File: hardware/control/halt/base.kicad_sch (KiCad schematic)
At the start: 0 parts

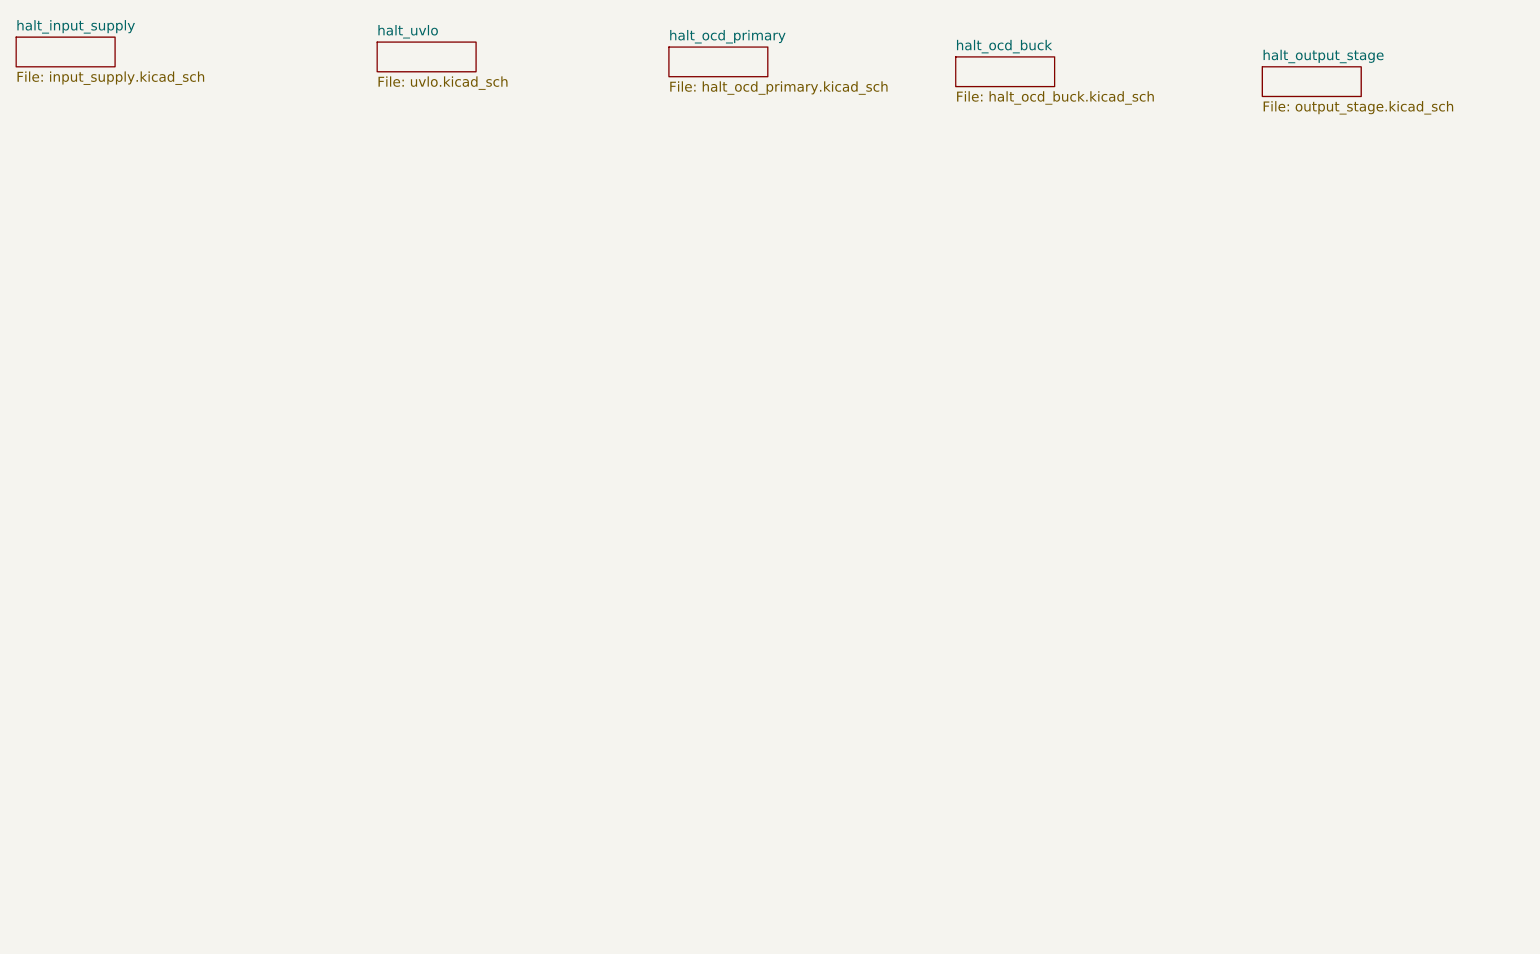
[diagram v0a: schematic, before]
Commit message: add progress on main drive controller and switch to hiearchical labels
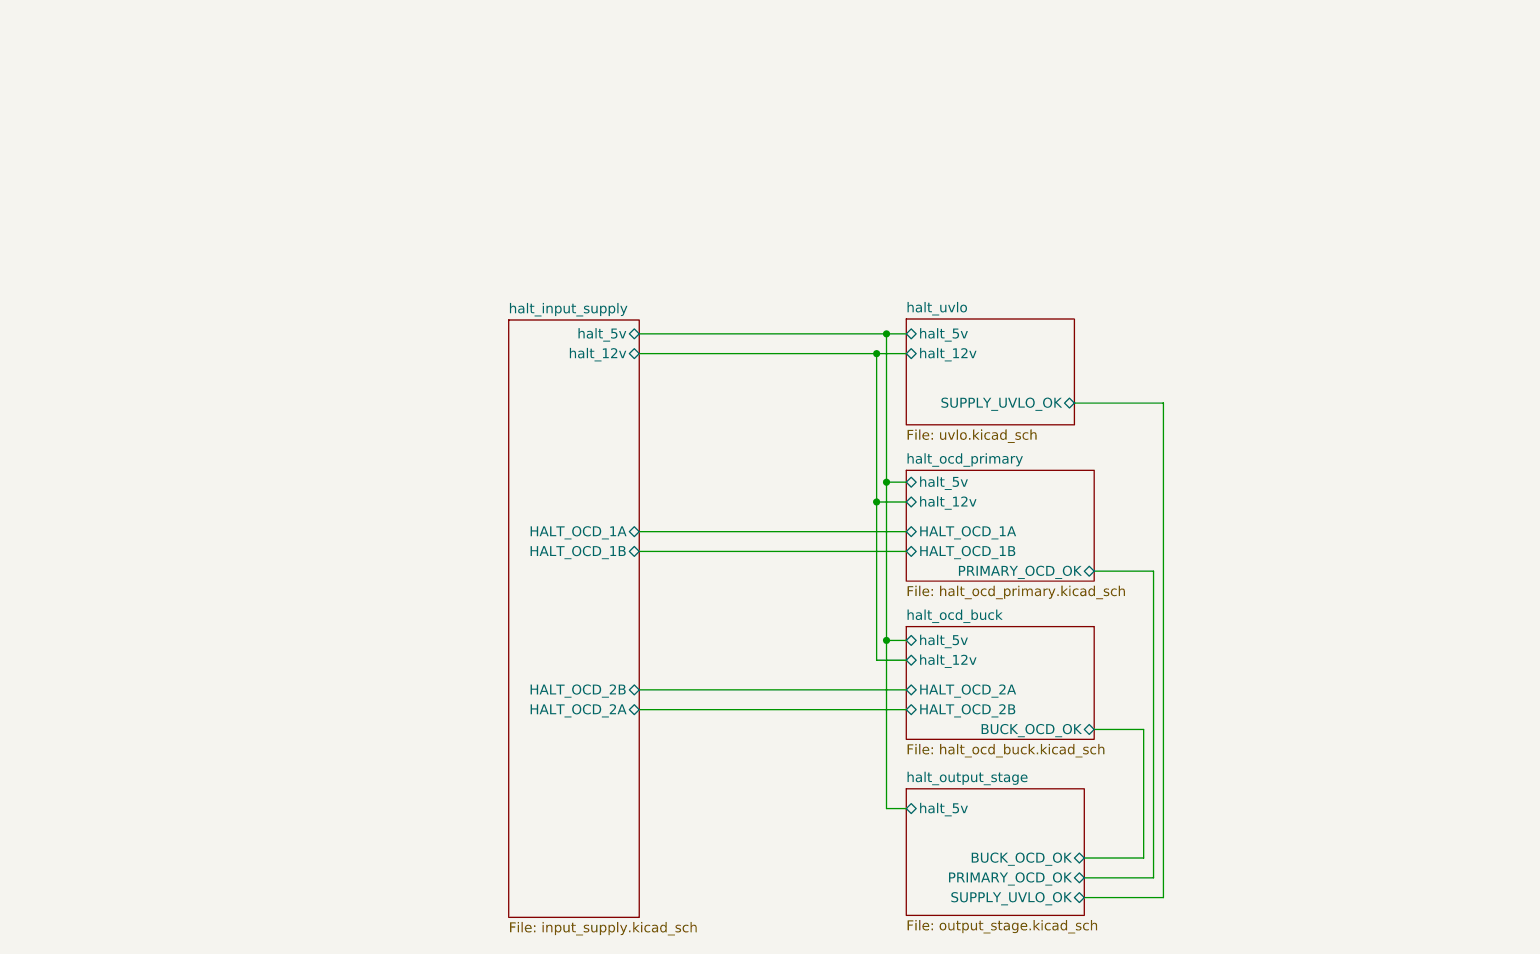
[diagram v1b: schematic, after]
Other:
- sheet halt_input_supply ports: added HALT_OCD_1A, HALT_OCD_1B, HALT_OCD_2A, HALT_OCD_2B, halt_12v, halt_5v; removed none
- sheet halt_ocd_buck ports: added BUCK_OCD_OK, HALT_OCD_2A, HALT_OCD_2B, halt_12v, halt_5v; removed none
- sheet halt_ocd_primary ports: added HALT_OCD_1A, HALT_OCD_1B, PRIMARY_OCD_OK, halt_12v, halt_5v; removed none
- sheet halt_output_stage ports: added BUCK_OCD_OK, PRIMARY_OCD_OK, SUPPLY_UVLO_OK, halt_5v; removed none
- sheet halt_uvlo ports: added SUPPLY_UVLO_OK, halt_12v, halt_5v; removed none

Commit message: update right about freaking everything
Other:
- sheet halt_uvlo ports: added none; removed halt_12v
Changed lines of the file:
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@@
 		(color 0 0 0 0)
 	)
-	(junction
-		(at 134.62 67.31)
-		(diameter 0)
-		(color 0 0 0 0)
-	)
 	(wire
 		(pts
@@
 		(pts
 			(xy 104.14 90.17) (xy 138.43 90.17)
-		)
-		(stroke
-			(width 0)
-			(type default)
-		)
-	)
-	(wire
-		(pts
-			(xy 134.62 67.31) (xy 138.43 67.31)
 		)
 		(stroke
@@
 			(effects
 				(font
-					(size 1.27 1.27)
-				)
-				(justify left)
-			)
-		)
-		(pin "halt_12v" bidirectional
-			(at 138.43 67.31 180)
-			(effects
-				(font
